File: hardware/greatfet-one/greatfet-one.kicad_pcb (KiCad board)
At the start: 4 copper layers, 70.6 x 53.3 mm, 99 parts, among them J1 NEIGHBOR1, J2 NEIGHBOR2, J3 USB-MICRO-B-SHIELDED, J4 USB-MICRO-B-SHIELDED, J5 JTAG, J6 POWER, J7 BONUS_ROW, SW1 DFU, SW2 RESET, U1 LPC4330FBD144, U2 W25Q16DV, U3 AP7333, U4 IP4220CZ6, U5 AP2553W6-7, X1 MCU_XTAL, X2 RTC_XTAL

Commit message: Restored VBUS voltage dividers which work correctly now that we learned how to turn off VBUS discharge in the microcontroller.
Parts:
- R21, R25: value 0 -> 10k
- R22, R26: value 10k -> 18k
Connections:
- J5 pad 7: (no net) -> Net-(J5-Pad7)
- U1 pad 136: (no net) -> Net-(U1-Pad136)
- U1 pad 138: (no net) -> Net-(U1-Pad138)
- U1 pad 139: (no net) -> Net-(U1-Pad139)
- U1 pad 142: (no net) -> Net-(U1-Pad142)
- U1 pad 2: (no net) -> Net-(U1-Pad2)
- U4 pad 4: (no net) -> Net-(U4-Pad4)
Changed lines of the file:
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@@
     (links 374)
     (no_connects 0)
-    (area 93.424104 68.58 207.466001 127.000001)
+    (area 105.842999 71.044999 176.605001 124.535001)
     (thickness 1.6)
     (drawings 230)
@@
     (zones 0)
     (modules 99)
-    (nets 134)
+    (nets 141)
   )
   (page A4)
@@
   (net 132 /USB0_VBUS)
   (net 133 /USB0_SENSE)
+  (net 134 "Net-(J5-Pad7)")
+  (net 135 "Net-(U1-Pad2)")
+  (net 136 "Net-(U1-Pad136)")
+  (net 137 "Net-(U1-Pad138)")
+  (net 138 "Net-(U1-Pad139)")
+  (net 139 "Net-(U1-Pad142)")
+  (net 140 "Net-(U4-Pad4)")
   (net_class Default "This is the default net class."
     (clearance 0.1524)
@@
     (add_net "Net-(J4-Pad2)")
     (add_net "Net-(J4-Pad3)")
+    (add_net "Net-(J5-Pad7)")
     (add_net "Net-(R13-Pad1)")
     (add_net "Net-(R23-Pad2)")
+    (add_net "Net-(U1-Pad136)")
+    (add_net "Net-(U1-Pad138)")
+    (add_net "Net-(U1-Pad139)")
+    (add_net "Net-(U1-Pad142)")
+    (add_net "Net-(U1-Pad2)")
+    (add_net "Net-(U4-Pad4)")
     (add_net VCC)
   )
@@
     (pad 3 smd rect (at 0.95 1.2 180) (size 0.55 0.8) (layers F.Cu F.Paste F.Mask)
       (net 92 /USB0_ID))
-    (pad 4 smd rect (at 0.95 -1.2 180) (size 0.55 0.8) (layers F.Cu F.Paste F.Mask))
+    (pad 4 smd rect (at 0.95 -1.2 180) (size 0.55 0.8) (layers F.Cu F.Paste F.Mask)
+      (net 140 "Net-(U4-Pad4)"))
     (pad 5 smd rect (at 0 -1.2 180) (size 0.55 0.8) (layers F.Cu F.Paste F.Mask)
       (net 132 /USB0_VBUS))
@@
       (net 98 /TDO) (die_length -2147.483648))
     (pad 7 thru_hole circle (at 1.27 0.635) (size 1.0668 1.0668) (drill 0.7112) (layers *.Cu *.Mask)
-      (die_length 0.08128))
+      (net 134 "Net-(J5-Pad7)") (die_length 0.08128))
     (pad 8 thru_hole circle (at 1.27 -0.635) (size 1.0668 1.0668) (drill 0.7112) (layers *.Cu *.Mask)
       (net 99 /TDI) (die_length -2147.483648))
@@
       (net 62 /P4_0) (die_length 0.01524))
     (pad 2 smd rect (at -11.00074 -8.24992) (size 1.50114 0.29464) (layers F.Cu F.Paste F.Mask)
-      (die_length 18.20672))
+      (net 135 "Net-(U1-Pad2)") (die_length 18.20672))
     (pad 3 smd rect (at -11.00074 -7.74954) (size 1.50114 0.29464) (layers F.Cu F.Paste F.Mask)
       (net 11 /LED2) (die_length 0.01524))
@@
       (net 1 GND) (die_length -2147.483648))
     (pad 136 smd rect (at -4.7498 -11.00074 90) (size 1.50114 0.29464) (layers F.Cu F.Paste F.Mask)
-      (die_length -2147.483648))
+      (net 136 "Net-(U1-Pad136)") (die_length -2147.483648))
     (pad 137 smd rect (at -5.25018 -11.00074 90) (size 1.50114 0.29464) (layers F.Cu F.Paste F.Mask)
       (net 4 VCC) (die_length 0.12192))
     (pad 138 smd rect (at -5.75056 -11.00074 90) (size 1.50114 0.29464) (layers F.Cu F.Paste F.Mask)
-      (die_length 0.01524))
+      (net 137 "Net-(U1-Pad138)") (die_length 0.01524))
     (pad 139 smd rect (at -6.25094 -11.00074 90) (size 1.50114 0.29464) (layers F.Cu F.Paste F.Mask)
-      (die_length -2147.483648))
+      (net 138 "Net-(U1-Pad139)") (die_length -2147.483648))
     (pad 140 smd rect (at -6.74878 -11.00074 90) (size 1.50114 0.29464) (layers F.Cu F.Paste F.Mask)
       (net 63 /P7_7) (die_length -2147.483648))
@@
       (net 4 VCC) (die_length -2147.483648))
     (pad 142 smd rect (at -7.74954 -11.00074 90) (size 1.50114 0.29464) (layers F.Cu F.Paste F.Mask)
-      (die_length 0.01524))
+      (net 139 "Net-(U1-Pad142)") (die_length 0.01524))
     (pad 143 smd rect (at -8.24992 -11.00074 90) (size 1.50114 0.29464) (layers F.Cu F.Paste F.Mask)
       (net 104 /ADC0_2) (die_length 18.20672))
@@
       (effects (font (size 0.6096 0.6096) (thickness 0.1524)))
     )
-    (fp_text value 0 (at 0 0 180) (layer F.SilkS) hide
+    (fp_text value 10k (at 0 0 180) (layer F.SilkS) hide
       (effects (font (size 0.6096 0.6096) (thickness 0.1524)))
     )
@@
       (effects (font (size 0.6096 0.6096) (thickness 0.1524)))
     )
-    (fp_text value 10k (at 0 0 270) (layer F.SilkS) hide
+    (fp_text value 18k (at 0 0 270) (layer F.SilkS) hide
       (effects (font (size 0.6096 0.6096) (thickness 0.1524)))
     )
@@
       (effects (font (size 0.6096 0.6096) (thickness 0.1524)))
     )
-    (fp_text value 0 (at 0 0) (layer F.SilkS) hide
+    (fp_text value 10k (at 0 0) (layer F.SilkS) hide
       (effects (font (size 0.6096 0.6096) (thickness 0.1524)))
     )
@@
       (effects (font (size 0.6096 0.6096) (thickness 0.1524)))
     )
-    (fp_text value 10k (at 0 0) (layer F.SilkS) hide
-      (effects (font (size 0.6096 0.6096) (thickness 0.1524)))
-    )
+    (fp_text value 18k (at 0 0) (layer F.SilkS) hide
+      (effects (font (size 0.6096 0.6096) (thickness 0.1524)))
+    )

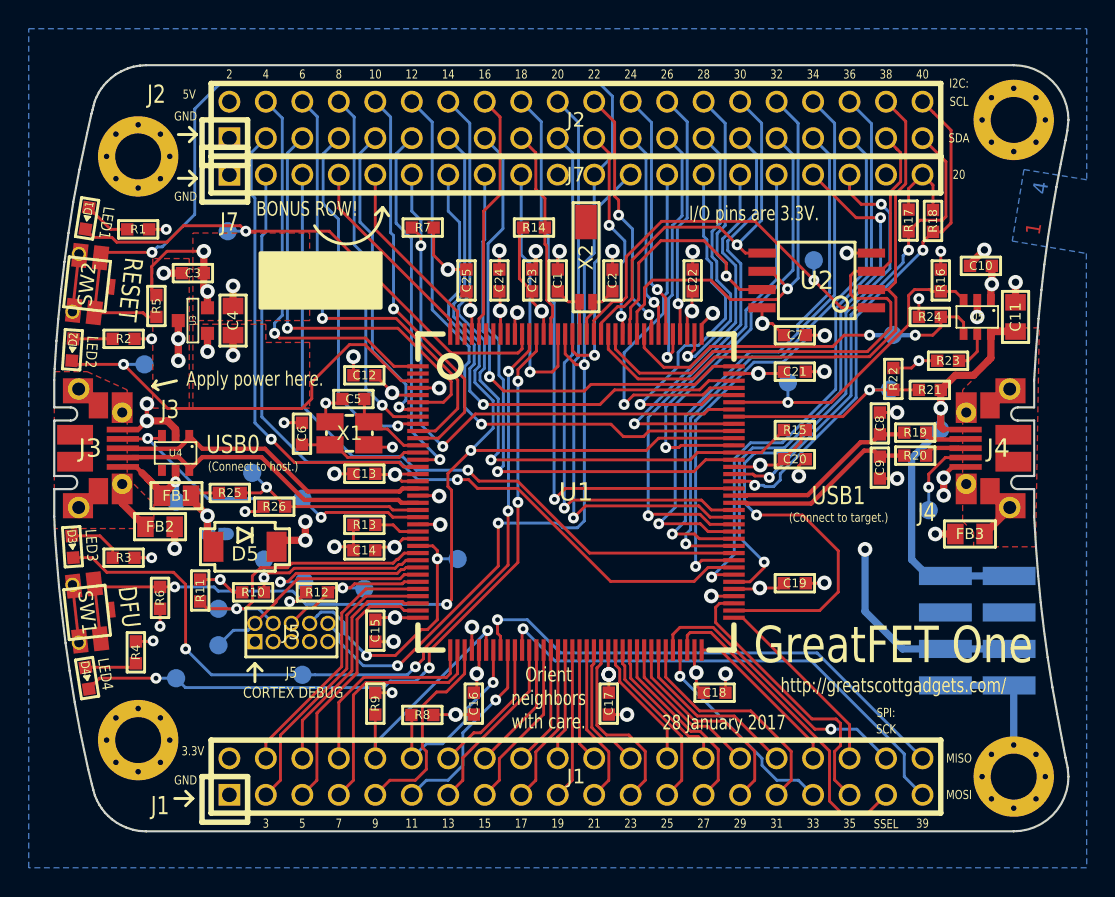
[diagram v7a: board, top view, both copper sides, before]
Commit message: GreatFET One: added 15k pull-down resistors to USB signals to support host mode
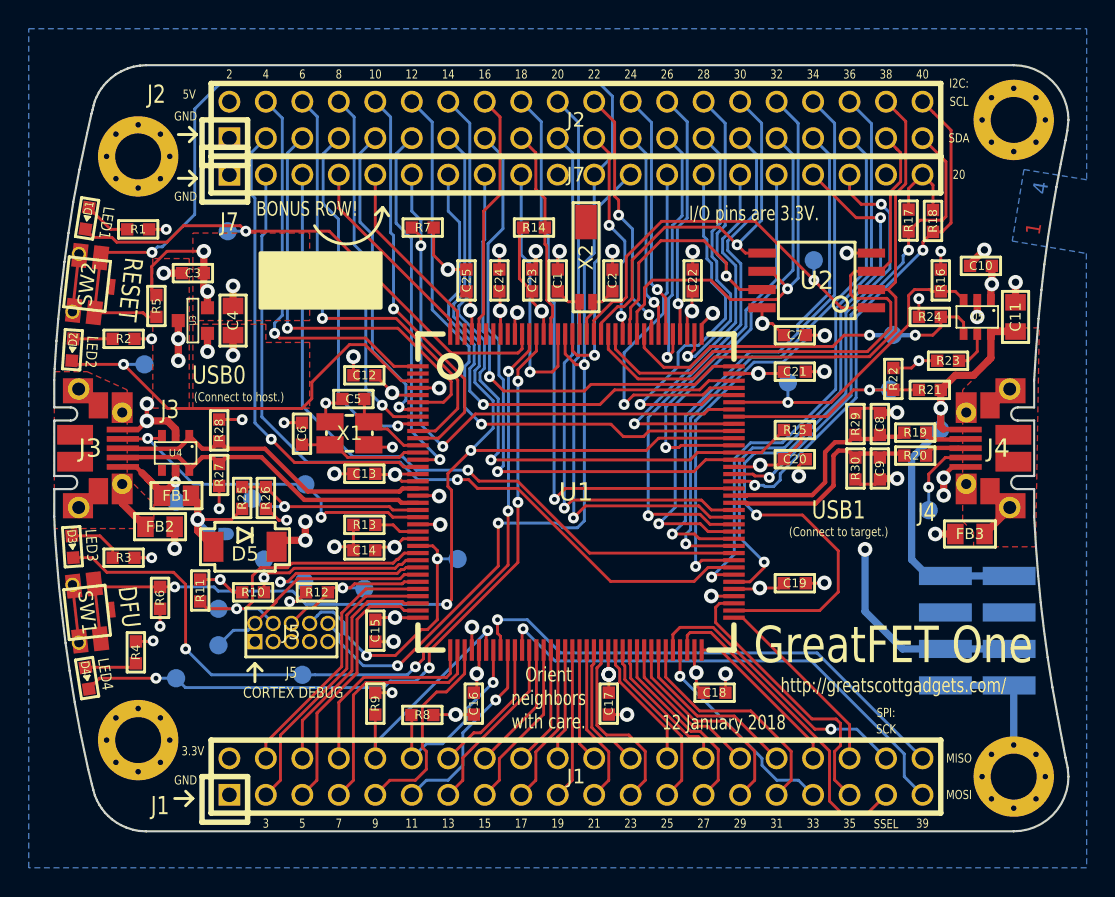
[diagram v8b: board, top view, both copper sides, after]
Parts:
- added R27: 15k, gsg-modules:0603, F.Cu at (117.4, 99.7)
- added R28: 15k, gsg-modules:0603, F.Cu at (117.4, 96.5)
- added R29: 15k, gsg-modules:0603, F.Cu at (161.7, 96.1)
- added R30: 15k, gsg-modules:0603, F.Cu at (161.7, 99.2)
- moved TP15 1.80 mm to (119.7, 101.3)
- moved TP13 1.02 mm to (123.4, 100.3)
- moved R25 0.93 mm to (119.0, 101.2), turned to 90 degrees
- moved R26 0.84 mm to (120.7, 101.2), turned to 90 degrees
- moved C9 0.06 mm to (163.4, 99.2)
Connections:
- J5 pad 7: Net-(J5-Pad7) -> (no net)
- U1 pad 136: Net-(U1-Pad136) -> (no net)
- U1 pad 138: Net-(U1-Pad138) -> (no net)
- U1 pad 139: Net-(U1-Pad139) -> (no net)
- U1 pad 142: Net-(U1-Pad142) -> (no net)
- U1 pad 2: Net-(U1-Pad2) -> (no net)
- U4 pad 4: Net-(U4-Pad4) -> (no net)
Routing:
- net GND: track 93.6 -> 101.1 mm, vias 47 -> 49
- net Net-(D5-Pad2): track 7.48 -> 9.49 mm
- net /USB1_D-: track 13.7 -> 15.4 mm
- net /USB1_D+: track 13.6 -> 15.3 mm
- net /USB0_SENSE: track 14.6 -> 15.4 mm
- net /USB0_ID: track 24.2 -> 24.9 mm
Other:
- board text added: "12 January 2018"
- board text added: "Use wiggler to remove neighbors."
- board text removed: "28 January 2017"
- board text removed: "Use lever to remove neighbors."
